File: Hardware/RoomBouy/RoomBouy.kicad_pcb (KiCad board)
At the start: 2 copper layers, 65 x 56.5 mm, 34 parts, among them J1 Roomba Wake, J2 Raspberry_Pi_2_3, J3 Roomba Connector, J4 ProtoPad, J5 Servo, Q1 MMBT3904, Q2 MMBT3904, Q3 MMBT3906, Q4 MMBT3904, Q6 MMBT3906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

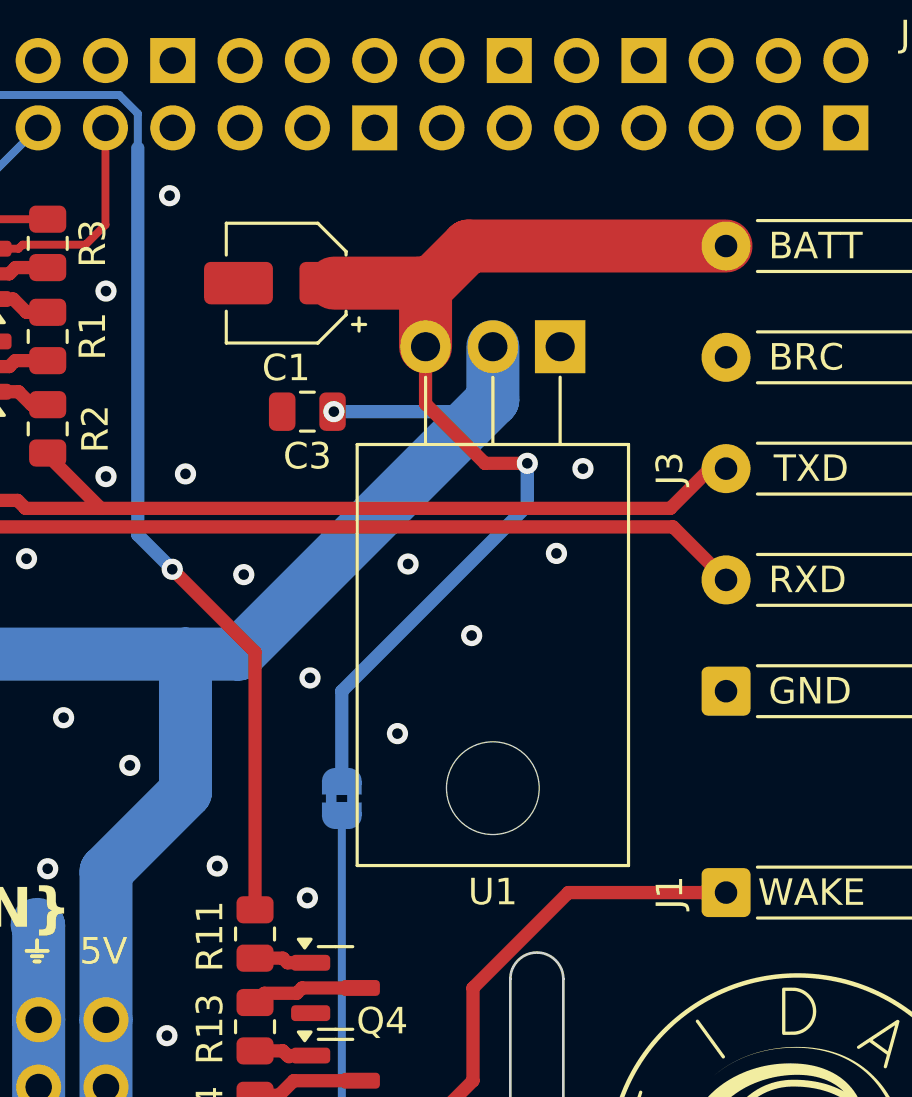
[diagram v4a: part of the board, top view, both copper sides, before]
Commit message: Add a low-voltage protection circuit (to protect against over-discharging roomba batteries
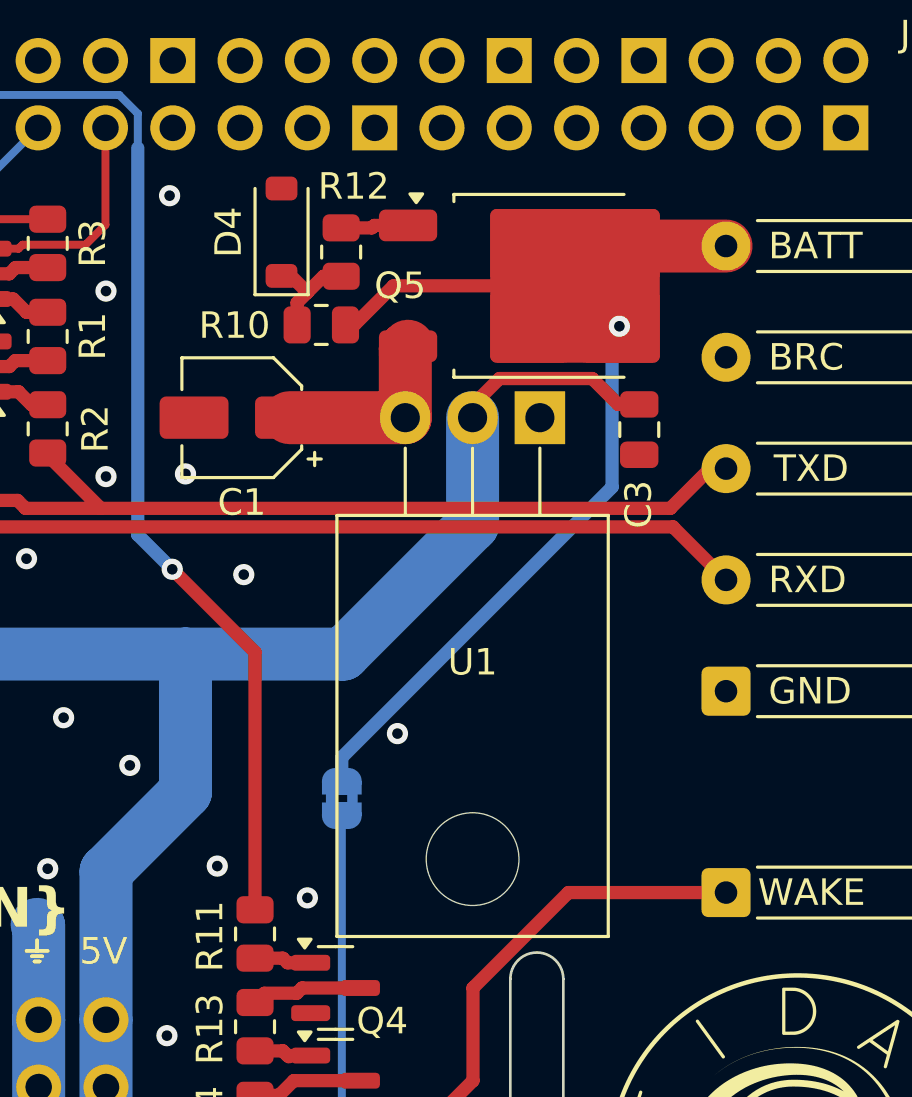
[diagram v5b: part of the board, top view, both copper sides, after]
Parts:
- added D4: BZT52C12V, Diode_SMD:D_SOD-123, F.Cu at (3.02, -19.5)
- added Q5: 2SB772, Package_TO_SOT_SMD:TO-252-2, F.Cu at (12.8, -17.5)
- added R10: 10k, Resistor_SMD:R_0805_2012Metric, F.Cu at (4.53, -16.0)
- added R12: 1k, Resistor_SMD:R_0805_2012Metric, F.Cu at (5.28, -18.8)
- moved C3 12.5 mm to (16.5, -12.1), turned to -90 degrees
- moved C1 5.35 mm to (1.52, -12.5)
- moved U1 2.78 mm to (12.8, -12.5)
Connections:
- C1 pad 1: +BATT -> Net-(Q5-C)
- J3 pad 4: /ROOMBA_BRC -> unconnected-(J3-Pin_4-Pad4)
- U1 pad 3: +BATT -> Net-(Q5-C)
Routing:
- net Net-(Q5-C): track 0.00 -> 7.11 mm
- net +BATT: track 39.6 -> 34.8 mm
- net Net-(D4-K): track 0.00 -> 4.15 mm
- net Net-(Q5-B): track 0.00 -> 2.56 mm
- net +5V: track 125.5 -> 126.2 mm, vias 3 -> 2
- net GND: vias 28 -> 23

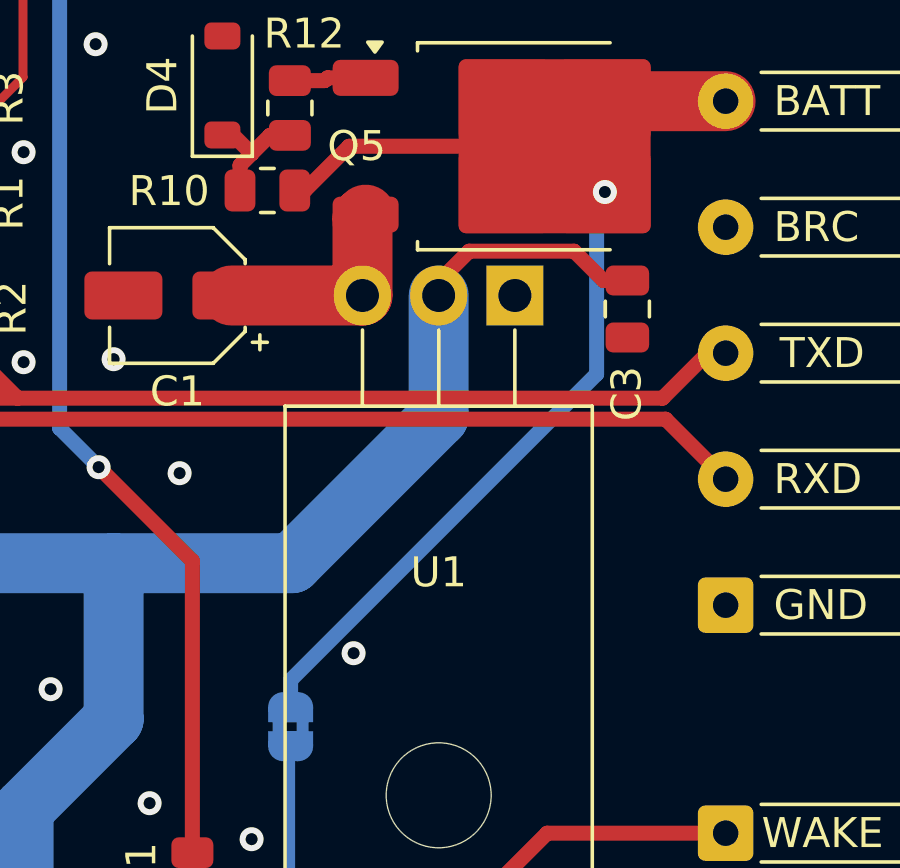
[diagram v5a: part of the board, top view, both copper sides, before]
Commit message: Fix switched power
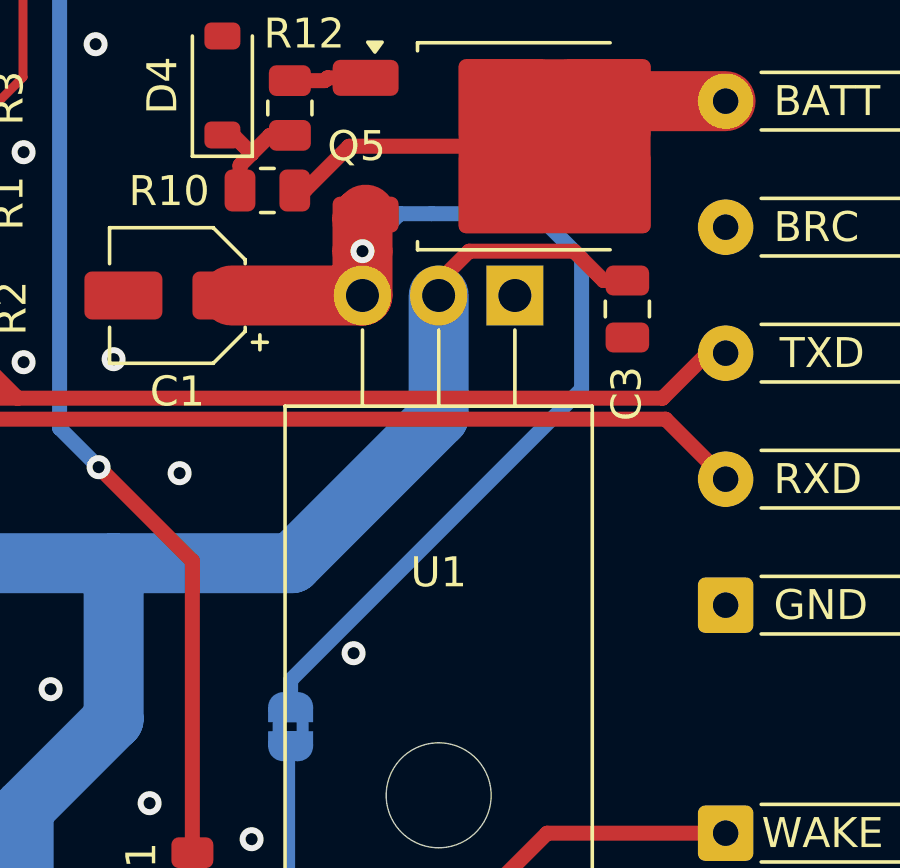
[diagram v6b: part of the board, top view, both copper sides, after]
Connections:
- C1 pad 1: Net-(Q5-C) -> /SWITCHED_BATT
- JP1 pad 2: +BATT -> /SWITCHED_BATT
- Q5 pad 3: Net-(Q5-C) -> /SWITCHED_BATT
- U1 pad 3: Net-(Q5-C) -> /SWITCHED_BATT
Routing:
- net /SWITCHED_BATT: track 0.00 -> 34.5 mm, vias 0 -> 1
- net +BATT: track 34.8 -> 13.3 mm, vias 1 -> 0
- net Net-(Q5-C): track 7.11 -> 0.00 mm
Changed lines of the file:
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@@
 	(net 51 "/SERVO")
 	(net 52 "unconnected-(J3-Pin_4-Pad4)")
-	(net 53 "Net-(Q5-C)")
+	(net 53 "/SWITCHED_BATT")
 	(net 54 "Net-(D4-K)")
 	(net 55 "Net-(Q5-B)")
@@
 			(layers "F.Cu" "F.Paste" "F.Mask")
 			(roundrect_rratio 0.15625)
-			(net 53 "Net-(Q5-C)")
+			(net 53 "/SWITCHED_BATT")
 			(pintype "passive")
 		)
@@
 			(layers "*.Cu" "*.Mask")
 			(remove_unused_layers no)
-			(net 53 "Net-(Q5-C)")
+			(net 53 "/SWITCHED_BATT")
 			(pinfunction "VI")
 			(pintype "power_in")
@@
 		(tags "resistor")
 		(property "Reference" "R10"
-			(at -3.275 0.0225 360)
+			(at -3.275 0.0225 0)
 			(layer "F.SilkS")
 			(effects
@@
 		)
 		(property "Value" "10k"
-			(at 0 1.65 360)
+			(at 0 1.65 0)
 			(layer "F.Fab")
 			(effects
@@
 		)
 		(fp_text user "${REFERENCE}"
-			(at 0 0 360)
+			(at 0 0 0)
 			(layer "F.Fab")
 			(effects
@@
 			(layers "F.Cu" "F.Paste" "F.Mask")
 			(roundrect_rratio 0.208333)
-			(net 53 "Net-(Q5-C)")
+			(net 53 "/SWITCHED_BATT")
 			(pinfunction "C")
 			(pintype "passive")
@@
 			(size 1 0.5)
 			(layers "B.Cu" "B.Mask")
-			(net 26 "+BATT")
+			(net 53 "/SWITCHED_BATT")
 			(pinfunction "B")
 			(pintype "passive")
@@
 		(net 26)
 	)
-	(via
-		(at 15.775 -15.9725)
-		(size 0.8)
-		(drill 0.4)
-		(layers "F.Cu" "B.Cu")
-		(net 26)
-	)
-	(segment
-		(start 15.5 -9.902082)
-		(end 15.5 -15.6975)
-		(width 0.5)
-		(layer "B.Cu")
-		(net 26)
-	)
-	(segment
-		(start 5.3 1.2)
-		(end 5.3 0.297918)
-		(width 0.5)
-		(layer "B.Cu")
-		(net 26)
-	)
-	(segment
-		(start 5.3 0.297918)
-		(end 15.5 -9.902082)
-		(width 0.5)
-		(layer "B.Cu")
-		(net 26)
-	)
-	(segment
-		(start 15.5 -15.6975)
-		(end 15.775 -15.9725)
-		(width 0.5)
-		(layer "B.Cu")
-		(net 26)
-	)
 	(segment
 		(start -6.9375 -9.4)
@@
 	)
 	(segment
+		(start 7.695 -14)
+		(end 7.695 -15.1125)
+		(width 2)
+		(layer "F.Cu")
+		(net 53)
+	)
+	(segment
 		(start 7.695 -15.1125)
 		(end 7.8 -15.2175)
@@
 	(segment
 		(start 7.695 -12.5225)
-		(end 7.695 -15.1125)
+		(end 7.695 -14)
 		(width 2)
 		(layer "F.Cu")
 		(net 53)
 	)
+	(via
+		(at 7.695 -14)
+		(size 0.8)
+		(drill 0.4)
+		(layers "F.Cu" "B.Cu")
+		(net 53)
+	)
+	(segment
+		(start 8.945 -15.25)
+		(end 7.695 -14)
+		(width 0.5)
+		(layer "B.Cu")
+		(net 53)
+	)
+	(segment
+		(start 15 -9.402082)
+		(end 15 -13.75)
+		(width 0.5)
+		(layer "B.Cu")
+		(net 53)
+	)
+	(segment
+		(start 13.5 -15.25)
+		(end 10 -15.25)
+		(width 0.5)
+		(layer "B.Cu")
+		(net 53)
+	)
+	(segment
+		(start 15 -13.75)
+		(end 13.5 -15.25)
+		(width 0.5)
+		(layer "B.Cu")
+		(net 53)
+	)
+	(segment
+		(start 10 -15.25)
+		(end 8.945 -15.25)
+		(width 0.5)
+		(layer "B.Cu")
+		(net 53)
+	)
+	(segment
+		(start 5.3 1.2)
+		(end 5.3 0.297918)
+		(width 0.5)
+		(layer "B.Cu")
+		(net 53)
+	)
+	(segment
+		(start 5.3 0.297918)
+		(end 15 -9.402082)
+		(width 0.5)
+		(layer "B.Cu")
+		(net 53)
+	)

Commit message: Bump rpi_hat_template
Co-Authored By: @devbisme
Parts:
- J5: footprint Connector_JST:JST_PH_S3B-PH-K_1x03_P2.00mm_Horizontal -> Connector_JST:JST_EH_S3B-EH_1x03_P2.50mm_Horizontal
- moved J5 4.53 mm to (-25.0, -14.8), turned to 90 degrees
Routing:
- net +5V: track 126.2 -> 116.6 mm
- net /SERVO: track 21.9 -> 21.4 mm
- net GND: vias 23 -> 22
